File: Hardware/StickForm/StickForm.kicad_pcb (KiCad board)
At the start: 2 copper layers, 51.5 x 20 mm, 62 parts, among them J1 48037-0001, J2 JTAG, J3 SWD, U1 SRV05-4, U10 SRV05-4, U11 SRV05-4, U2 STM32L432KBU6, U3 ME6211A33M3G-N, U4 AD8531ARTZ, U5 74AVCH2T45DC, U6 74LVC2G125, U7 74LVC2G125, U8 74LVC2G125, U9 74LVC2G125, Y1 32768 7pF

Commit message: Updated Glossy MSP430 device (Stick Form)
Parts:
- moved C11 2.24 mm to (71.0, 63.5), turned to 180 degrees
- moved R5 2.24 mm to (73.2, 63.5), turned to 180 degrees
- moved R6 2.24 mm to (73.2, 59.2), turned to 180 degrees
- moved C12 2.21 mm to (71.0, 59.2), turned to 0 degrees
- moved C3 2.19 mm to (86.5, 68.3)
- moved Y1 1.10 mm to (84.3, 68.5)
- moved C8 1.03 mm to (75.8, 55.8), turned to 90 degrees
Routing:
- net GND: track 27.8 -> 63.3 mm, vias 7 -> 14
- net /TVref: track 19.1 -> 51.5 mm, vias 1 -> 3
- net /mTCK: track 5.73 -> 37.6 mm, vias 0 -> 3
- net /SBWO: track 5.27 -> 37.0 mm, vias 0 -> 2
- net /mTMS: track 8.89 -> 40.1 mm, vias 1 -> 2
- net /mTDO: track 0.00 -> 30.4 mm, vias 0 -> 2
- net /ENA2N: track 9.03 -> 37.5 mm, vias 1 -> 4
- net /ENA1N: track 9.29 -> 36.3 mm, vias 2 -> 4
- net /mRXD: track 0.00 -> 25.2 mm, vias 0 -> 2
- net /LEDS: track 0.00 -> 23.3 mm, vias 0 -> 2
- net /SWDIO: track 0.00 -> 22.2 mm, vias 0 -> 2
- net +3V3: track 1.05 -> 22.7 mm, vias 0 -> 2
- net /SWCLK: track 0.00 -> 20.2 mm, vias 0 -> 2
- net /mTDI: track 7.73 -> 27.8 mm, vias 0 -> 2
- net /NRST: track 0.00 -> 19.2 mm, vias 0 -> 2
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
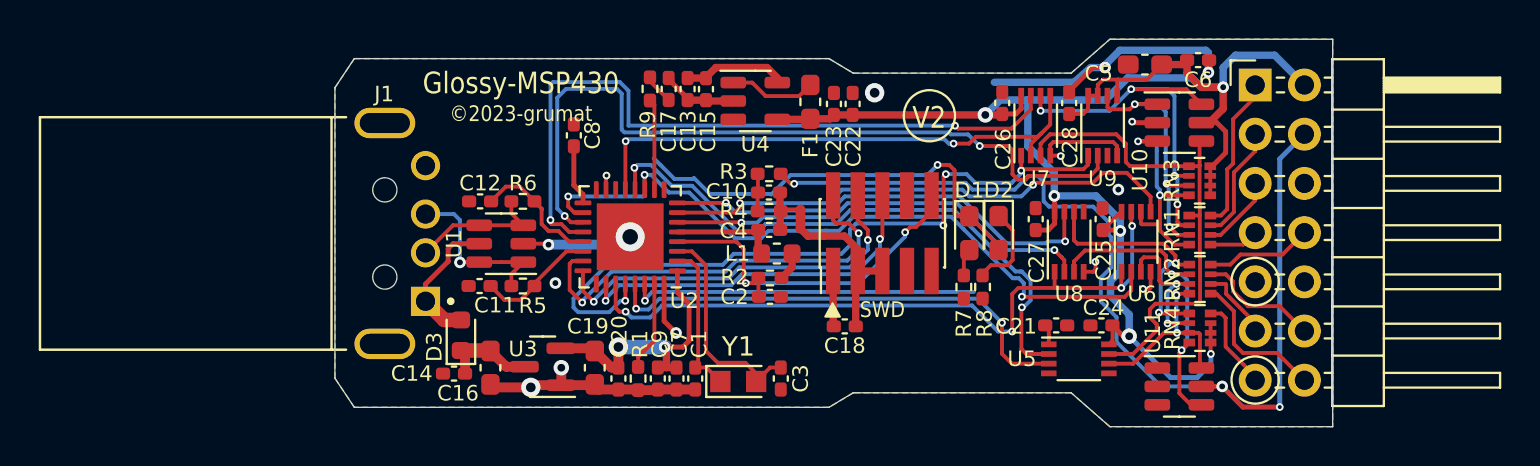
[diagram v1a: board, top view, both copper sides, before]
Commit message: Updated Stick Form Glossy MSP430 device
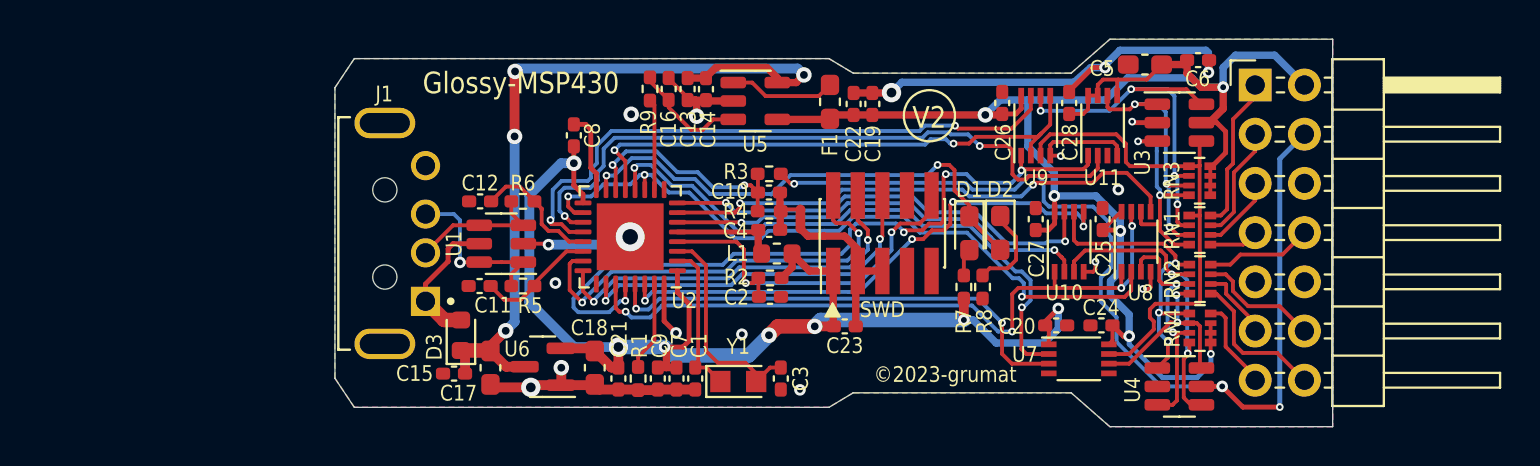
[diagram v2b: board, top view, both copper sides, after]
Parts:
- moved C19 1.02 mm to (91.2, 54.1)
- moved C22 1.02 mm to (90.3, 54.1)
- moved F1 1.02 mm to (89.1, 54.0)
- moved D2 0.09 mm to (97.8, 60.8)
- renumbered C15 to C14, C14 to C15, C17 to C16, C16 to C17, C19 to C18, C22 to C19, C21 to C20, C20 to C21, C23 to C22, C18 to C23, U8 to U10, U9 to U11, U10 to U3, U11 to U4, U4 to U5, U3 to U6, U5 to U7, U6 to U8, U7 to U9
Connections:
- RN4 pad 2: /rRST -> /rRXD
- RN4 pad 3: /rRXD -> /rRST
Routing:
- net +3V3: track 22.7 -> 65.6 mm, vias 2 -> 7
- net +5V: track 10.3 -> 41.9 mm, vias 0 -> 4
- net GND: track 63.3 -> 75.9 mm, vias 14 -> 18
- net /VREF_2: track 1.95 -> 12.0 mm, vias 0 -> 2
- net /mTXD: track 18.1 -> 27.8 mm, vias 1 -> 4
- net /SBWO: track 37.0 -> 31.7 mm
- net /mTMS: track 40.1 -> 34.9 mm
- net /rRST: track 7.77 -> 12.8 mm
- net Net-(C16-Pad1): track 1.56 -> 5.99 mm
- net /rTEST: track 12.8 -> 16.1 mm, vias 2 -> 3
- net /LEDS: track 23.3 -> 25.7 mm
- net Net-(F1-Pad2): track 4.51 -> 5.52 mm
- net /mTCK: track 37.6 -> 36.9 mm
- net /mTDI: track 27.8 -> 28.3 mm
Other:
- rule pad_to_mask_clearance: 0.1 -> 0

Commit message: Updated schematics for StickForm (WIP)
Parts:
- removed R2: 100K, Resistor_SMD:R_0402_1005Metric_Pad0.72x0.64mm_HandSolder
- moved C2 0.99 mm to (86.0, 63.1)
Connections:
- U1 pad 1: /HUSBP -> unconnected-(U1-Pad1)
- U1 pad 3: /HUSBM -> unconnected-(U1-Pad3)
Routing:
- net /HUSBP: track 8.86 -> 7.26 mm
- net /HUSBM: track 7.13 -> 5.53 mm
- net +3V3: track 65.6 -> 64.1 mm
- net /NRST: track 19.6 -> 18.7 mm
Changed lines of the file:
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@@
   (net 60 "/mTXD")
   (net 61 "unconnected-(U11-Pad3)")
+  (net 62 "unconnected-(U1-Pad1)")
+  (net 63 "unconnected-(U1-Pad3)")
   (footprint "Lib:MOLEX_48037-0001" locked (layer "F.Cu")
     (at 66.075 60.825 -90)
@@
   )
   (footprint "Capacitor_SMD:C_0402_1005Metric_Pad0.74x0.62mm_HandSolder" (layer "F.Cu")
-    (at 85.9536 64.0969)
+    (at 85.9536 63.1063)
     (descr "Capacitor SMD 0402 (1005 Metric), square (rectangular) end terminal, IPC_7351 nominal with elongated pad for handsoldering. (Body size source: IPC-SM-782 page 76, https://www.pcb-3d.com/wordpress/wp-content/uploads/ipc-sm-782a_amendment_1_and_2.pdf), generated with kicad-footprint-generator")
     (tags "capacitor handsolder")
@@
     )
   )
-  (footprint "Resistor_SMD:R_0402_1005Metric_Pad0.72x0.64mm_HandSolder" (layer "F.Cu")
-    (at 85.9536 63.1219)
-    (descr "Resistor SMD 0402 (1005 Metric), square (rectangular) end terminal, IPC_7351 nominal with elongated pad for handsoldering. (Body size source: IPC-SM-782 page 72, https://www.pcb-3d.com/wordpress/wp-content/uploads/ipc-sm-782a_amendment_1_and_2.pdf), generated with kicad-footprint-generator")
-    (tags "resistor handsolder")
-    (property "Descr" "100kΩ ±1% 1/16W ±100ppm/℃ 0402 Chip Resistor - Surface Mount RoHS")
-    (property "LCSC" "C25741")
-    (property "Sheetfile" "StickForm.kicad_sch")
-    (property "Sheetname" "")
-    (attr smd)
-    (fp_text reference "R2" (at -1.7272 -0.041 180) (layer "F.SilkS")
-      (effects (font (size 0.8128 0.7112) (thickness 0.15)))
-    )
-    (fp_text value "100K" (at 0 1.17) (layer "F.Fab")
-      (effects (font (size 1 1) (thickness 0.15)))
-    )
-    (fp_text user "${REFERENCE}" (at 0 0) (layer "F.Fab")
-      (effects (font (size 0.8128 0.7112) (thickness 0.1524)))
-    )
-    (fp_line (start -0.167621 -0.38) (end 0.167621 -0.38) (layer "F.SilkS") (width 0.12))
-    (fp_line (start -0.167621 0.38) (end 0.167621 0.38) (layer "F.SilkS") (width 0.12))
-    (fp_line (start -1.1 0.47) (end -1.1 -0.47) (layer "F.CrtYd") (width 0.05))
-    (fp_line (start 1.1 0.47) (end -1.1 0.47) (layer "F.CrtYd") (width 0.05))
-    (fp_line (start 1.1 -0.47) (end 1.1 0.47) (layer "F.CrtYd") (width 0.05))
-    (fp_line (start -1.1 -0.47) (end 1.1 -0.47) (layer "F.CrtYd") (width 0.05))
-    (fp_line (start 0.525 -0.27) (end 0.525 0.27) (layer "F.Fab") (width 0.1))
-    (fp_line (start -0.525 0.27) (end -0.525 -0.27) (layer "F.Fab") (width 0.1))
-    (fp_line (start -0.525 -0.27) (end 0.525 -0.27) (layer "F.Fab") (width 0.1))
-    (fp_line (start 0.525 0.27) (end -0.525 0.27) (layer "F.Fab") (width 0.1))
-    (pad "1" smd roundrect locked (at -0.5975 0) (size 0.715 0.64) (layers "F.Cu" "F.Paste" "F.Mask") (roundrect_rratio 0.25)
-      (net 7 "/NRST") (pintype "passive"))
-    (pad "2" smd roundrect locked (at 0.5975 0) (size 0.715 0.64) (layers "F.Cu" "F.Paste" "F.Mask") (roundrect_rratio 0.25)
-      (net 3 "+3V3") (pintype "passive"))
-    (model "${KICAD6_3DMODEL_DIR}/Resistor_SMD.3dshapes/R_0402_1005Metric.wrl"
-      (offset (xyz 0 0 0))
-      (scale (xyz 1 1 1))
-      (rotate (xyz 0 0 0))
-    )
-  )
   (footprint "Capacitor_SMD:C_0402_1005Metric_Pad0.74x0.62mm_HandSolder" (layer "F.Cu")
     (at 80.7256 53.3656 90)
@@
     (fp_line (start -0.8 -1.05) (end -0.4 -1.45) (layer "F.Fab") (width 0.1))
     (pad "1" smd roundrect (at -1.1375 -0.95 180) (size 1.325 0.6) (layers "F.Cu" "F.Paste" "F.Mask") (roundrect_rratio 0.25)
-      (net 39 "/HUSBP") (pinfunction "IO1") (pintype "passive"))
+      (net 62 "unconnected-(U1-Pad1)") (pinfunction "IO1") (pintype "passive+no_connect"))
     (pad "2" smd roundrect (at -1.1375 0 180) (size 1.325 0.6) (layers "F.Cu" "F.Paste" "F.Mask") (roundrect_rratio 0.25)
       (net 1 "GND") (pinfunction "VN") (pintype "passive"))
     (pad "3" smd roundrect (at -1.1375 0.95 180) (size 1.325 0.6) (layers "F.Cu" "F.Paste" "F.Mask") (roundrect_rratio 0.25)
-      (net 40 "/HUSBM") (pinfunction "IO2") (pintype "passive"))
+      (net 63 "unconnected-(U1-Pad3)") (pinfunction "IO2") (pintype "passive+no_connect"))
     (pad "4" smd roundrect (at 1.1375 0.95 180) (size 1.325 0.6) (layers "F.Cu" "F.Paste" "F.Mask") (roundrect_rratio 0.25)
       (net 40 "/HUSBM") (pinfunction "IO3") (pintype "passive"))
@@
   (segment (start 80.6109 67.7458) (end 81.1296 67.7458) (width 0.381) (layer "F.Cu") (net 3))
   (segment (start 87.9975 62.7625) (end 87.0967 61.8617) (width 0.381) (layer "F.Cu") (net 3))
-  (segment (start 86.5511 63.1219) (end 87.0967 62.5763) (width 0.381) (layer "F.Cu") (net 3))
   (segment (start 76.3025 59.2481) (end 76.3025 58.809) (width 0.254) (layer "F.Cu") (net 3))
   (segment (start 75.1563 66.7537) (end 76.7729 66.7537) (width 0.508) (layer "F.Cu") (net 3))
@@
   (segment (start 100.3461 65.756) (end 100.1602 65.5701) (width 0.2) (layer "F.Cu") (net 3))
   (segment (start 78.1304 67.7458) (end 77.765 67.7458) (width 0.508) (layer "F.Cu") (net 3))
-  (segment (start 87.0967 61.8617) (end 87.0967 62.5763) (width 0.381) (layer "F.Cu") (net 3))
   (segment (start 81.4558 66.6877) (end 81.781 66.3625) (width 0.254) (layer "F.Cu") (net 3))
   (segment (start 80.1644 67.7458) (end 80.6109 67.7458) (width 0.381) (layer "F.Cu") (net 3))
@@
   (segment (start 85.2424 68.0593) (end 85.2424 68.4657) (width 0.2) (layer "F.Cu") (net 6))
   (segment (start 93.6754 60.3125) (end 93.6757 60.3128) (width 0.2) (layer "F.Cu") (net 7))
-  (segment (start 85.0905 63.3875) (end 85.3561 63.1219) (width 0.2) (layer "F.Cu") (net 7))
   (segment (start 84.2166 61.2481) (end 84.606 61.6375) (width 0.2) (layer "F.Cu") (net 7))
   (segment (start 92.6774 60.3125) (end 93.6754 60.3125) (width 0.2) (layer "F.Cu") (net 7))
+  (segment (start 85.1049 63.3875) (end 85.3861 63.1063) (width 0.2) (layer "F.Cu") (net 7))
   (segment (start 92.2274 60.7625) (end 92.6774 60.3125) (width 0.2) (layer "F.Cu") (net 7))
   (segment (start 84.606 61.6375) (end 84.606 63.2875) (width 0.2) (layer "F.Cu") (net 7))
-  (segment (start 85.3561 64.0669) (end 85.3861 64.0969) (width 0.2) (layer "F.Cu") (net 7))
-  (segment (start 85.3561 63.1219) (end 85.3561 64.0669) (width 0.2) (layer "F.Cu") (net 7))
   (segment (start 81.1775 61.2481) (end 84.2166 61.2481) (width 0.2) (layer "F.Cu") (net 7))
   (segment (start 93.6757 60.3128) (end 94.296 59.6925) (width 0.2) (layer "F.Cu") (net 7))
-  (segment (start 84.706 63.3875) (end 85.0905 63.3875) (width 0.2) (layer "F.Cu") (net 7))
   (segment (start 94.296 59.6925) (end 94.296 58.8625) (width 0.2) (layer "F.Cu") (net 7))
   (segment (start 84.606 63.2875) (end 84.706 63.3875) (width 0.2) (layer "F.Cu") (net 7))
+  (segment (start 84.706 63.3875) (end 85.1049 63.3875) (width 0.2) (layer "F.Cu") (net 7))
   (via (at 84.706 63.3875) (size 0.4) (drill 0.2) (layers "F.Cu" "B.Cu") (net 7))
   (via (at 92.2274 60.7625) (size 0.4) (drill 0.2) (layers "F.Cu" "B.Cu") (net 7))
@@
   (segment (start 110.236 61.9125) (end 112.4097 61.9125) (width 0.2) (layer "F.Cu") (net 38))
   (segment (start 112.4097 61.9125) (end 113.54 60.7822) (width 0.2) (layer "F.Cu") (net 38))
-  (segment (start 72.6053 63.5381) (end 72.6053 62.9211) (width 0.2) (layer "F.Cu") (net 39))
   (segment (start 70.9477 62.3037) (end 69.9668 62.3037) (width 0.2) (layer "F.Cu") (net 39))
-  (segment (start 72.1004 62.3037) (end 70.9477 62.3037) (width 0.2) (layer "F.Cu") (net 39))
-  (segment (start 72.6053 62.9211) (end 73.2227 62.3037) (width 0.2) (layer "F.Cu") (net 39))
+  (segment (start 71.3709 62.3037) (end 72.6053 63.5381) (width 0.2) (layer "F.Cu") (net 39))
+  (segment (start 70.9477 62.3037) (end 71.3709 62.3037) (width 0.2) (layer "F.Cu") (net 39))
   (segment (start 69.9668 62.3037) (end 69.9516 62.3189) (width 0.2) (layer "F.Cu") (net 39))
-  (segment (start 73.2227 62.3037) (end 72.1004 62.3037) (width 0.2) (layer "F.Cu") (net 39))
   (via (at 69.9516 62.3189) (size 0.6) (drill 0.3) (layers "F.Cu" "B.Cu") (net 39))
   (segment (start 69.9516 62.3189) (end 69.9516 60.1345) (width 0.2) (layer "B.Cu") (net 39))
@@
   (segment (start 69.9516 60.1345) (end 69.6421 59.825) (width 0.2) (layer "B.Cu") (net 39))
   (segment (start 69.5963 60.4037) (end 70.9477 60.4037) (width 0.2) (layer "F.Cu") (net 40))
-  (segment (start 72.6053 59.7863) (end 73.2227 60.4037) (width 0.2) (layer "F.Cu") (net 40))
-  (segment (start 73.2227 60.4037) (end 70.9477 60.4037) (width 0.2) (layer "F.Cu") (net 40))
-  (segment (start 72.6053 59.1693) (end 72.6053 59.7863) (width 0.2) (layer "F.Cu") (net 40))
+  (segment (start 70.9477 60.4037) (end 71.3709 60.4037) (width 0.2) (layer "F.Cu") (net 40))
+  (segment (start 71.3709 60.4037) (end 72.6053 59.1693) (width 0.2) (layer "F.Cu") (net 40))
   (segment (start 68.175 61.825) (end 69.5963 60.4037) (width 0.2) (layer "F.Cu") (net 40))
   (segment (start 90.486 58.8625) (end 90.481 58.8675) (width 0.2) (layer "F.Cu") (net 41))
